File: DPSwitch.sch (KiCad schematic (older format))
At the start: 43 parts, among them J1 USB_OTG, J2 USB_OTG, J3 DP_47272, J4 DP_47272, J5 DP_47272, J6 USB_A, SW1 SEL_A, SW2 SEL_B, U1 HD3SS215, U2 74LVC2G00DC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

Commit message: Rev1 for manufacture
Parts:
- removed D1, D2: D_Small, Diodes_SMD:D_SC-80_HandSoldering, symbol device:D_Small
- added D1, D2: BAT54GWJ, Diodes_SMD:D_SOD-123, symbol visclib:BAT54GWJ
- C16: footprint Capacitors_SMD:C_0603_HandSoldering -> Capacitors_SMD:C_0805_HandSoldering
- D4: footprint LEDs:LED_0603_HandSoldering -> Visclib:wolfpaw-0.3-illuminated
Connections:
- net VDD: now also D1.1 (K), D2.1 (K)
- net at J2.1 (VBUS): now also D2.2 (A)
- net at J1.1 (VBUS): now also D1.2 (A)
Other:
- note added: "!! 4GHz Routing !!\n\n50R ±15% Single Ended\n100R ±20% Differential\n\n6mils Wide\n8mils Gap\n20mils Between pairs"
- note added: "LOGO"
- note removed: "!! 4GHz Routing !!\n\n50R ±15% Single Ended\n100R ±20% Differential\n\n5mils Wide\n7mils Gap\n20mils Between pairs"
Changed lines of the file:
@@
 $EndDescr
-$Comp
-L visclib:HD3SS215 U1
-U 1 1 5FCC9A98
-P 5400 1750
-F 0 "U1" H 4500 1550 50  0000 C CNN
-F 1 "HD3SS215" H 5350 1100 50  0000 C CNN
-F 2 "Visclib:VQFN-56_EP_7.8x7.8_Pitch0.5mm" H 5250 1750 50  0001 C CNN
-F 3 "" H 5250 1750 50  0001 C CNN
-	1    5400 1750
-	1    0    0    -1
-$EndComp
 $Comp
 L device:R_Small_US R5
@@
 F 0 "D4" H 5693 595 50  0000 C CNN
 F 1 "PWR" H 5693 686 50  0000 C CNN
-F 2 "LEDs:LED_0603_HandSoldering" H 5700 850 50  0001 C CNN
+F 2 "Visclib:wolfpaw-0.3-illuminated" H 5700 850 50  0001 C CNN
 F 3 "~" H 5700 850 50  0001 C CNN
 	1    5700 850
@@
 Text Notes 1200 3350 1    50   ~ 0
 TODO: VERIFY PINOUT
-$Comp
-L device:D_Small D1
-U 1 1 5FD305A8
-P 1850 850
-F 0 "D1" H 1850 645 50  0000 C CNN
-F 1 "D_Small" H 1850 736 50  0000 C CNN
-F 2 "Diodes_SMD:D_SC-80_HandSoldering" V 1850 850 50  0001 C CNN
-F 3 "~" V 1850 850 50  0001 C CNN
-	1    1850 850
-	-1   0    0    1
-$EndComp
 $Comp
 L visclib:V_IN #PWR0101
@@
 TODO: VERIFY PINOUT
 $Comp
-L device:D_Small D2
-U 1 1 5FDA8E27
-P 1850 6950
-F 0 "D2" H 1850 6745 50  0000 C CNN
-F 1 "D_Small" H 1850 6836 50  0000 C CNN
-F 2 "Diodes_SMD:D_SC-80_HandSoldering" V 1850 6950 50  0001 C CNN
-F 3 "~" V 1850 6950 50  0001 C CNN
-	1    1850 6950
-	-1   0    0    1
-$EndComp
-$Comp
 L visclib:V_IN #PWR0106
 U 1 1 5FDA8E33
@@
 DX_SEL L=DFPA H=DFPB
 Wire Wire Line
-	1950 850  2100 850
-Wire Wire Line
 	2100 850  2100 750
 Wire Bus Line
@@
 Wire Notes Line
 	600  750  1050 750
-Wire Wire Line
-	1750 6950 1650 6950
-Wire Wire Line
-	2100 6950 1950 6950
 Wire Bus Line
 	7100 2500 9550 2500
@@
 Wire Wire Line
 	8300 1300 8300 1150
-Wire Wire Line
-	8300 1150 8650 1150
 Connection ~ 8300 1150
 Wire Wire Line
@@
 Wire Wire Line
 	8050 2100 7550 2100
-Wire Wire Line
-	8650 1650 8300 1650
 Wire Wire Line
 	8300 1150 8300 900
@@
 	1    0    0    -1
 $EndComp
-Connection ~ 8300 1650
 $Comp
 L regul:MCP1700-3302E_SOT23 U3
@@
 Wire Wire Line
 	2100 850  3950 850
-Connection ~ 2100 850
 $Comp
 L visclib:GND #PWR0102
@@
 F 0 "C16" H 5050 950 50  0000 R CNN
 F 1 "1u" H 5100 1050 50  0000 R CNN
-F 2 "Capacitors_SMD:C_0603_HandSoldering" H 4850 1000 50  0001 C CNN
+F 2 "Capacitors_SMD:C_0805_HandSoldering" H 4850 1000 50  0001 C CNN
 F 3 "~" H 4850 1000 50  0001 C CNN
 	1    4850 1000
@@
 Wire Wire Line
 	5550 850  5400 850
-Wire Bus Line
-	7100 2500 7100 4750
-Wire Bus Line
-	9550 1950 9550 2500
-Wire Bus Line
-	1950 7250 1950 7400
-Wire Bus Line
-	3950 6100 3950 7400
-Wire Bus Line
-	3950 3950 3950 4250
-Wire Bus Line
-	2100 1150 2100 1350
-Wire Bus Line
-	8300 2850 8300 4650
-Wire Bus Line
-	3850 4500 3850 6350
-Wire Bus Line
-	2900 4500 2900 6350
-Wire Bus Line
-	3850 2350 3850 4100
-Wire Bus Line
-	2900 1950 2900 4100
-Wire Bus Line
-	6950 2850 6950 4550
 Connection ~ 5400 850
 Text Notes 7250 3600 0    50   ~ 0
-!! 4GHz Routing !!\n\n50R ±15% Single Ended\n100R ±20% Differential\n\n5mils Wide\n7mils Gap\n20mils Between pairs
+!! 4GHz Routing !!\n\n50R ±15% Single Ended\n100R ±20% Differential\n\n6mils Wide\n8mils Gap\n20mils Between pairs
 Text Notes 4350 7500 0    50   ~ 0
 DP Routing Guide:\nhttps://www.nxp.com/docs/en/application-note/AN10798.pdf
+$Comp
+L visclib:HD3SS215 U1
+U 1 1 5FCC9A98
+P 5400 1750
+F 0 "U1" H 4500 1550 50  0000 C CNN
+F 1 "HD3SS215" H 5350 1100 50  0000 C CNN
+F 2 "Visclib:VQFN-56_EP_7.8x7.8_Pitch0.5mm" H 5250 1750 50  0001 C CNN
+F 3 "" H 5250 1750 50  0001 C CNN
+	1    5400 1750
+	1    0    0    -1
+$EndComp
+Connection ~ 2100 850
+$Comp
+L visclib:BAT54GWJ D2
+U 1 1 60E45C52
+P 1850 850
+F 0 "D2" H 1850 645 50  0000 C CNN
+F 1 "BAT54GWJ" H 1850 736 50  0000 C CNN
+F 2 "Diodes_SMD:D_SOD-123" V 1850 850 50  0001 C CNN
+F 3 "~" V 1850 850 50  0001 C CNN
+	1    1850 850
+	-1   0    0    1
+$EndComp
+$Comp
+L visclib:BAT54GWJ D1
+U 1 1 60E46CCE
+P 1750 6950
+F 0 "D1" H 1750 6745 50  0000 C CNN
+F 1 "BAT54GWJ" H 1750 6836 50  0000 C CNN
+F 2 "Diodes_SMD:D_SOD-123" V 1750 6950 50  0001 C CNN
+F 3 "~" V 1750 6950 50  0001 C CNN
+	1    1750 6950
+	-1   0    0    1
+$EndComp
+Wire Wire Line
+	1850 6950 2100 6950
+Wire Wire Line
+	1950 850  2100 850
+Wire Bus Line
+	7100 2500 7100 4750
+Wire Bus Line
+	9550 1950 9550 2500
+Wire Bus Line
+	1950 7250 1950 7400
+Wire Bus Line
+	3950 6100 3950 7400
+Wire Bus Line
+	3950 3950 3950 4250
+Wire Bus Line
+	2100 1150 2100 1350
+Wire Bus Line
+	8300 2850 8300 4650
+Wire Bus Line
+	3850 4500 3850 6350
+Wire Bus Line
+	2900 4500 2900 6350
+Wire Bus Line
+	6950 2850 6950 4550
+Wire Bus Line
+	3850 2350 3850 4100
+Wire Bus Line
+	2900 1950 2900 4100
+Connection ~ 8300 1650
+Wire Wire Line
+	8650 1650 8300 1650
+Wire Wire Line
+	8300 1150 8650 1150
+Text Notes 5600 1050 0    50   ~ 0
+LOGO
 $EndSCHEMATC

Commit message: Added moth
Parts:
- added LOGO1: Moth, Project:moth, symbol visclib:Logo
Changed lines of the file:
@@
 EESchema Schematic File Version 4
+LIBS:DPSwitch-cache
 EELAYER 29 0
 EELAYER END
@@
 U 1 1 5FCDBC5B
 P 5700 850
-F 0 "D4" H 5693 595 50  0000 C CNN
-F 1 "PWR" H 5693 686 50  0000 C CNN
-F 2 "Visclib:wolfpaw-0.3-illuminated" H 5700 850 50  0001 C CNN
+F 0 "D4" H 5700 750 50  0000 C CNN
+F 1 "PWR" H 5700 1000 50  0000 C CNN
+F 2 "Visclib:wolfpaw-0.3-illuminated" H 5600 550 50  0000 C CNN
 F 3 "~" H 5700 850 50  0001 C CNN
 	1    5700 850
@@
 Wire Wire Line
 	1950 850  2100 850
+Connection ~ 8300 1650
+Wire Wire Line
+	8650 1650 8300 1650
+Wire Wire Line
+	8300 1150 8650 1150
+Text Notes 5600 700  0    50   ~ 0
+LOGO
 Wire Bus Line
 	7100 2500 7100 4750
@@
 	2900 4500 2900 6350
 Wire Bus Line
+	3850 2350 3850 4100
+Wire Bus Line
+	2900 1950 2900 4100
+Wire Bus Line
 	6950 2850 6950 4550
-Wire Bus Line
-	3850 2350 3850 4100
-Wire Bus Line
-	2900 1950 2900 4100
-Connection ~ 8300 1650
-Wire Wire Line
-	8650 1650 8300 1650
-Wire Wire Line
-	8300 1150 8650 1150
-Text Notes 5600 1050 0    50   ~ 0
-LOGO
+$Comp
+L visclib:Logo LOGO1
+U 1 1 5FD38948
+P 10500 6850
+F 0 "LOGO1" H 10728 6903 60  0000 L CNN
+F 1 "Moth" H 10728 6797 60  0000 L CNN
+F 2 "Project:moth" H 10500 6850 60  0001 C CNN
+F 3 "" H 10500 6850 60  0001 C CNN
+	1    10500 6850
+	1    0    0    -1
+$EndComp
 $EndSCHEMATC

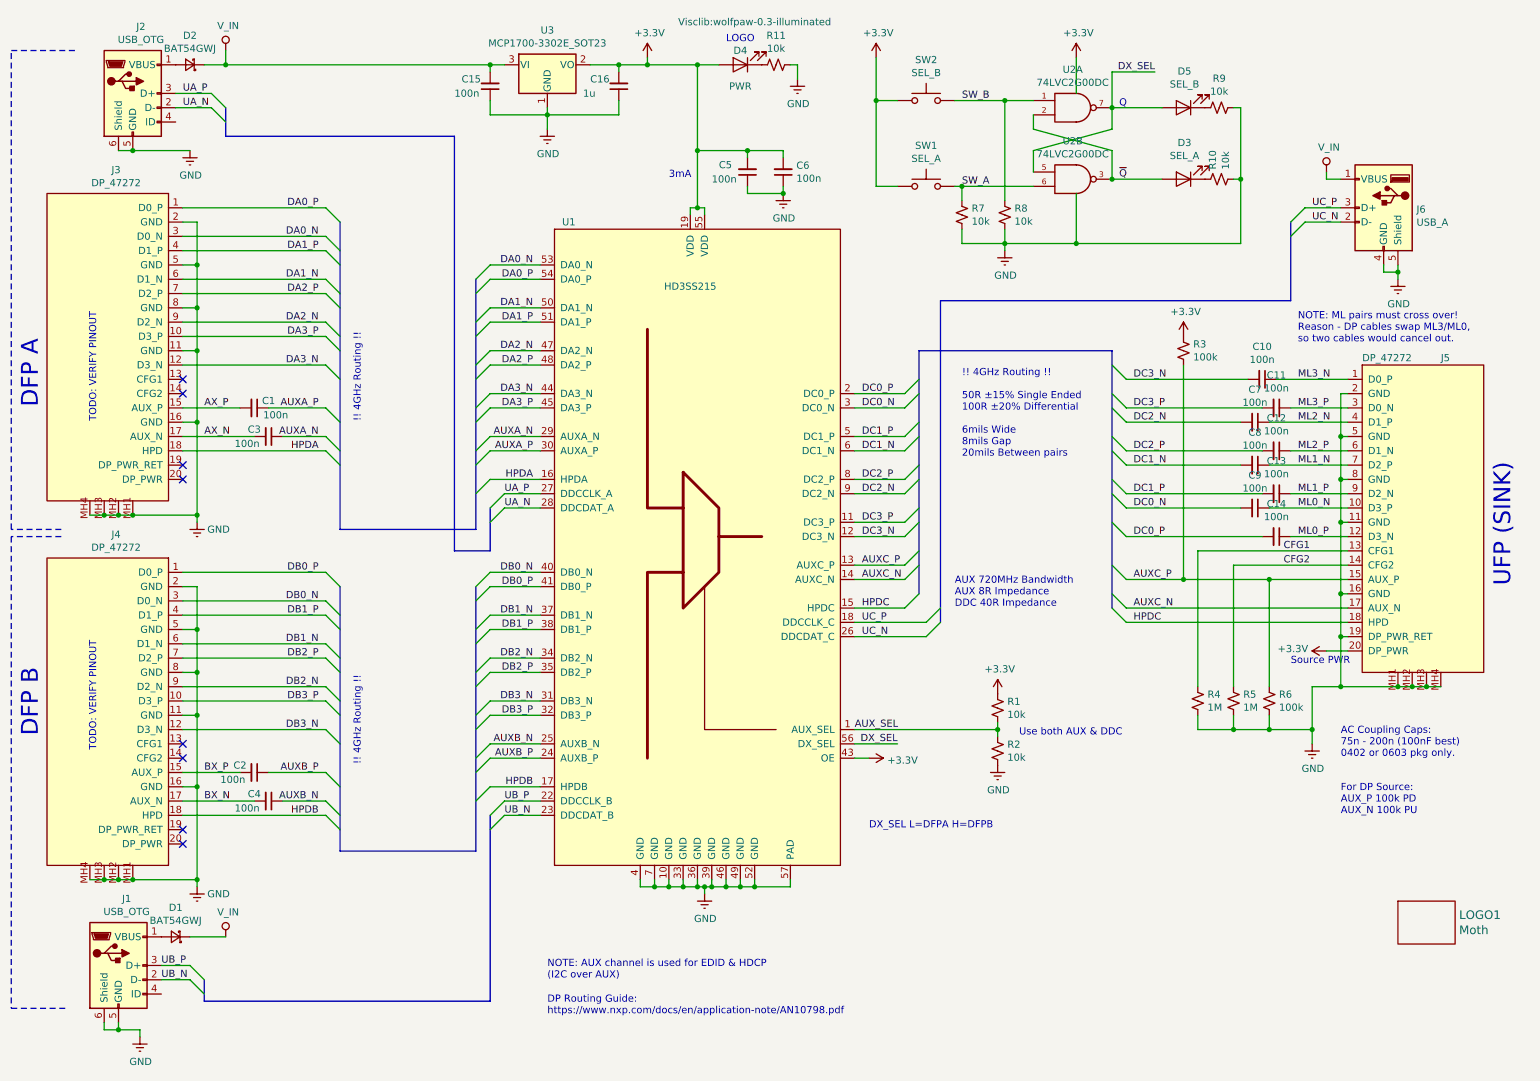
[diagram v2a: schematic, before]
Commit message: r2 - Swap USB A/B inputs, fix inverted flip-flop logic
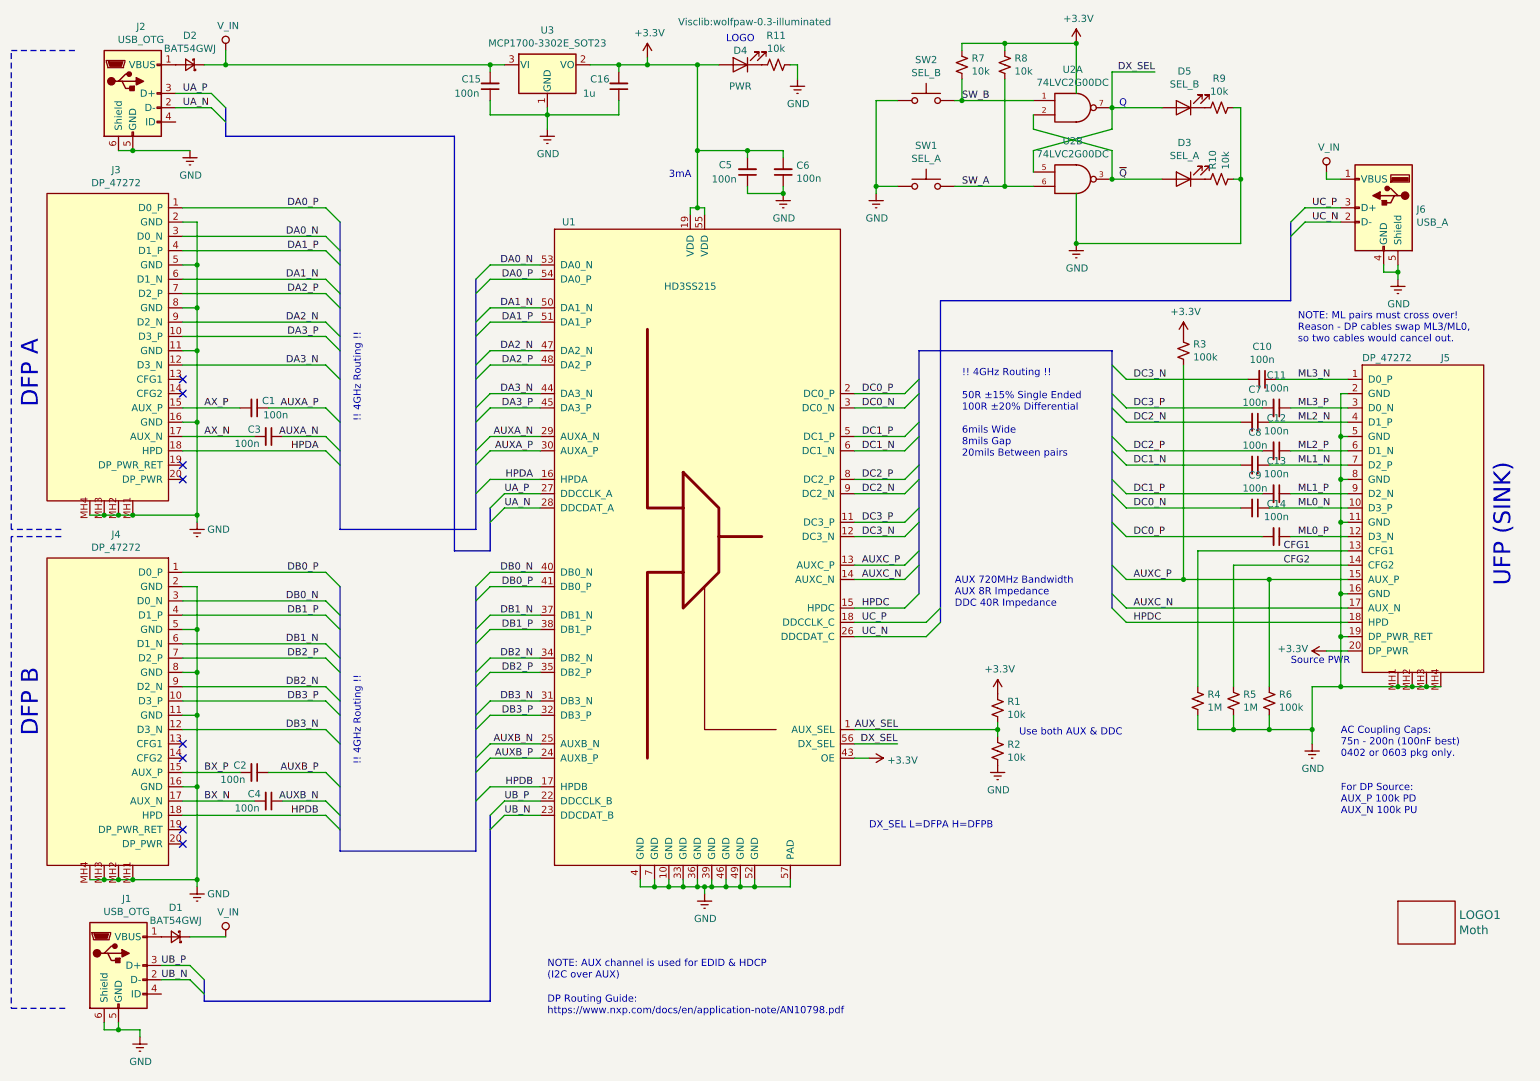
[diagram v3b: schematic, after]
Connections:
- net +3V3: now also R7.1, R8.1; no longer SW1.1, SW2.1
- net GND: now also SW1.1, SW2.1; no longer R7.2, R8.2
- net SW_A: now also R8.2; no longer R7.1
- net SW_B: now also R7.2; no longer R8.1
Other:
- note removed: "TODO: VERIFY PINOUT"
- moved on the sheet: R7, R8
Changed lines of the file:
@@
 	-1   0    0    -1
 $EndComp
-Text Notes 1200 3350 1    50   ~ 0
-TODO: VERIFY PINOUT
 $Comp
 L visclib:V_IN #PWR0101
@@
 	1    0    0    -1
 $EndComp
-Text Notes 1200 5650 1    50   ~ 0
-TODO: VERIFY PINOUT
 $Comp
 L visclib:V_IN #PWR0106
@@
 L power:+3.3V #PWR0119
 U 1 1 60A55216
-P 8050 800
-F 0 "#PWR0119" H 8050 650 50  0001 C CNN
-F 1 "+3.3V" H 8065 973 50  0000 C CNN
-F 2 "" H 8050 800 50  0001 C CNN
-F 3 "" H 8050 800 50  0001 C CNN
-	1    8050 800
-	1    0    0    -1
-$EndComp
-Wire Wire Line
-	8050 800  8050 1050
-Wire Wire Line
-	7200 1700 7250 1700
-Wire Wire Line
-	7200 1100 7550 1100
-$Comp
-L power:+3.3V #PWR0120
-U 1 1 60A8D1FA
-P 6650 800
-F 0 "#PWR0120" H 6650 650 50  0001 C CNN
-F 1 "+3.3V" H 6665 973 50  0000 C CNN
-F 2 "" H 6650 800 50  0001 C CNN
-F 3 "" H 6650 800 50  0001 C CNN
-	1    6650 800
-	1    0    0    -1
-$EndComp
-Wire Wire Line
-	6650 800  6650 1100
+P 8050 700
+F 0 "#PWR0119" H 8050 550 50  0001 C CNN
+F 1 "+3.3V" H 8065 873 50  0000 C CNN
+F 2 "" H 8050 700 50  0001 C CNN
+F 3 "" H 8050 700 50  0001 C CNN
+	1    8050 700
+	1    0    0    -1
+$EndComp
 Wire Wire Line
 	6650 1700 6800 1700
 Wire Wire Line
 	6800 1100 6650 1100
-Connection ~ 6650 1100
 Wire Wire Line
 	6650 1100 6650 1700
@@
 L device:R_Small_US R7
 U 1 1 60AB2679
-P 7250 1900
-F 0 "R7" H 7318 1946 50  0000 L CNN
-F 1 "10k" H 7318 1855 50  0000 L CNN
-F 2 "Resistors_SMD:R_0603_HandSoldering" H 7250 1900 50  0001 C CNN
-F 3 "~" H 7250 1900 50  0001 C CNN
-	1    7250 1900
+P 7250 850
+F 0 "R7" H 7318 896 50  0000 L CNN
+F 1 "10k" H 7318 805 50  0000 L CNN
+F 2 "Resistors_SMD:R_0603_HandSoldering" H 7250 850 50  0001 C CNN
+F 3 "~" H 7250 850 50  0001 C CNN
+	1    7250 850
 	1    0    0    -1
 $EndComp
@@
 L device:R_Small_US R8
 U 1 1 60AB2C26
-P 7550 1900
-F 0 "R8" H 7618 1946 50  0000 L CNN
-F 1 "10k" H 7618 1855 50  0000 L CNN
-F 2 "Resistors_SMD:R_0603_HandSoldering" H 7550 1900 50  0001 C CNN
-F 3 "~" H 7550 1900 50  0001 C CNN
-	1    7550 1900
-	1    0    0    -1
-$EndComp
-Wire Wire Line
-	7250 1800 7250 1700
-Connection ~ 7250 1700
-Wire Wire Line
-	7250 1700 7750 1700
-Wire Wire Line
-	7550 1800 7550 1100
-Connection ~ 7550 1100
-Wire Wire Line
-	7550 1100 7750 1100
-Wire Wire Line
-	7250 2000 7250 2100
-Wire Wire Line
-	7250 2100 7550 2100
-Wire Wire Line
-	7550 2100 7550 2000
+P 7550 850
+F 0 "R8" H 7618 896 50  0000 L CNN
+F 1 "10k" H 7618 805 50  0000 L CNN
+F 2 "Resistors_SMD:R_0603_HandSoldering" H 7550 850 50  0001 C CNN
+F 3 "~" H 7550 850 50  0001 C CNN
+	1    7550 850
+	1    0    0    -1
+$EndComp
 $Comp
 L visclib:GND #PWR0121
 U 1 1 60AEBFAE
-P 7550 2150
-F 0 "#PWR0121" H 7550 1900 50  0001 C CNN
-F 1 "GND" H 7555 1977 50  0000 C CNN
-F 2 "" H 7550 2150 50  0001 C CNN
-F 3 "" H 7550 2150 50  0001 C CNN
-	1    7550 2150
-	1    0    0    -1
-$EndComp
-Wire Wire Line
-	7550 2150 7550 2100
-Connection ~ 7550 2100
+P 8050 2100
+F 0 "#PWR0121" H 8050 1850 50  0001 C CNN
+F 1 "GND" H 8055 1927 50  0000 C CNN
+F 2 "" H 8050 2100 50  0001 C CNN
+F 3 "" H 8050 2100 50  0001 C CNN
+	1    8050 2100
+	1    0    0    -1
+$EndComp
 $Comp
 L device:R_Small_US R10
@@
 Wire Wire Line
 	8050 1750 8050 2100
-Connection ~ 8050 2100
-Wire Wire Line
-	8050 2100 7550 2100
 Wire Wire Line
 	8300 1150 8300 900
@@
 Text Notes 5600 700  0    50   ~ 0
 LOGO
-Wire Bus Line
-	7100 2500 7100 4750
-Wire Bus Line
-	9550 1950 9550 2500
-Wire Bus Line
-	1950 7250 1950 7400
-Wire Bus Line
-	3950 6100 3950 7400
-Wire Bus Line
-	3950 3950 3950 4250
-Wire Bus Line
-	2100 1150 2100 1350
-Wire Bus Line
-	8300 2850 8300 4650
-Wire Bus Line
-	3850 4500 3850 6350
-Wire Bus Line
-	2900 4500 2900 6350
-Wire Bus Line
-	3850 2350 3850 4100
-Wire Bus Line
-	2900 1950 2900 4100
-Wire Bus Line
-	6950 2850 6950 4550
 $Comp
 L visclib:Logo LOGO1
@@
 	1    0    0    -1
 $EndComp
+Wire Wire Line
+	7200 1700 7550 1700
+Wire Wire Line
+	7200 1100 7250 1100
+Wire Wire Line
+	7250 950  7250 1100
+Connection ~ 7250 1100
+Wire Wire Line
+	7250 1100 7750 1100
+Wire Wire Line
+	7550 950  7550 1700
+Connection ~ 7550 1700
+Wire Wire Line
+	7550 1700 7750 1700
+Wire Wire Line
+	7250 750  7250 700
+Wire Wire Line
+	7550 700  7550 750
+$Comp
+L visclib:GND #PWR?
+U 1 1 60089F24
+P 6650 1750
+F 0 "#PWR?" H 6650 1500 50  0001 C CNN
+F 1 "GND" H 6655 1577 50  0000 C CNN
+F 2 "" H 6650 1750 50  0001 C CNN
+F 3 "" H 6650 1750 50  0001 C CNN
+	1    6650 1750
+	1    0    0    -1
+$EndComp
+Wire Wire Line
+	6650 1750 6650 1700
+Connection ~ 6650 1700
+Connection ~ 8050 2100
+Wire Wire Line
+	7250 700  7550 700
+Wire Wire Line
+	7550 700  8050 700
+Wire Wire Line
+	8050 700  8050 1050
+Connection ~ 7550 700
+Connection ~ 8050 700
+Wire Bus Line
+	7100 2500 7100 4750
+Wire Bus Line
+	9550 1950 9550 2500
+Wire Bus Line
+	1950 7250 1950 7400
+Wire Bus Line
+	3950 6100 3950 7400
+Wire Bus Line
+	3950 3950 3950 4250
+Wire Bus Line
+	2100 1150 2100 1350
+Wire Bus Line
+	8300 2850 8300 4650
+Wire Bus Line
+	3850 4500 3850 6350
+Wire Bus Line
+	2900 4500 2900 6350
+Wire Bus Line
+	3850 2350 3850 4100
+Wire Bus Line
+	2900 1950 2900 4100
+Wire Bus Line
+	6950 2850 6950 4550
 $EndSCHEMATC
